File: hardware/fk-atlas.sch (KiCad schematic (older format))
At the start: 55 parts, among them J1 CONN-HDR-2x5, J2 MICRO-USB, J3 Conn_01x02, J4 Conn_01x09, M1 MOUNT_HOLE, M2 MOUNT_HOLE, M3 MOUNT_HOLE, M4 MOUNT_HOLE, Q1 2N7002LT1G, Q2 2N7002LT1G, Q3 2N7002LT1G, Q4 2N7002LT1G, Q5 2N7002LT1G, SW1 SPNO, U1 S25FL1xxK0XM, U2 ATSAMD21G18A-AU, U3 MCP1700T-3302E/MB, Y1 FC-135

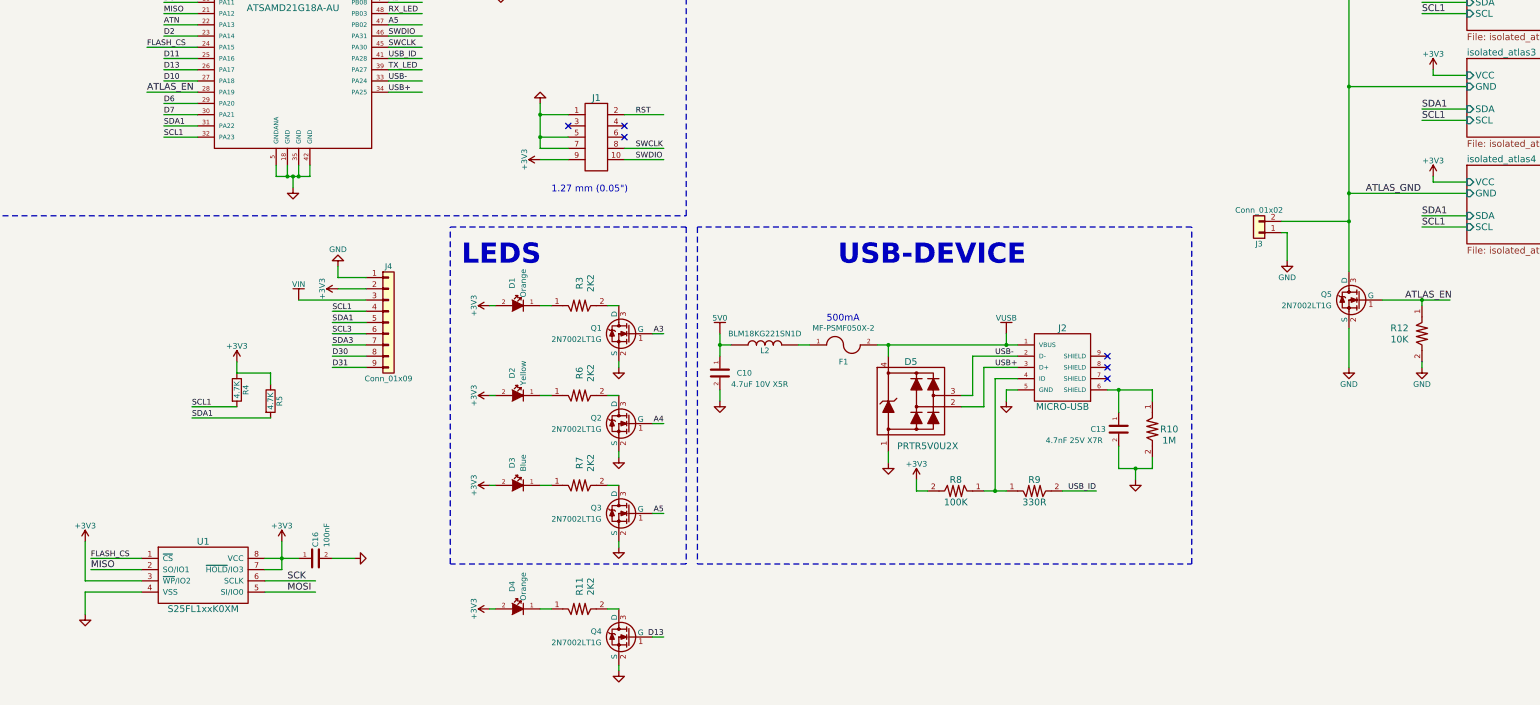
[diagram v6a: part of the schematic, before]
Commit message: Flash memory is on PERIPH_GND now too.
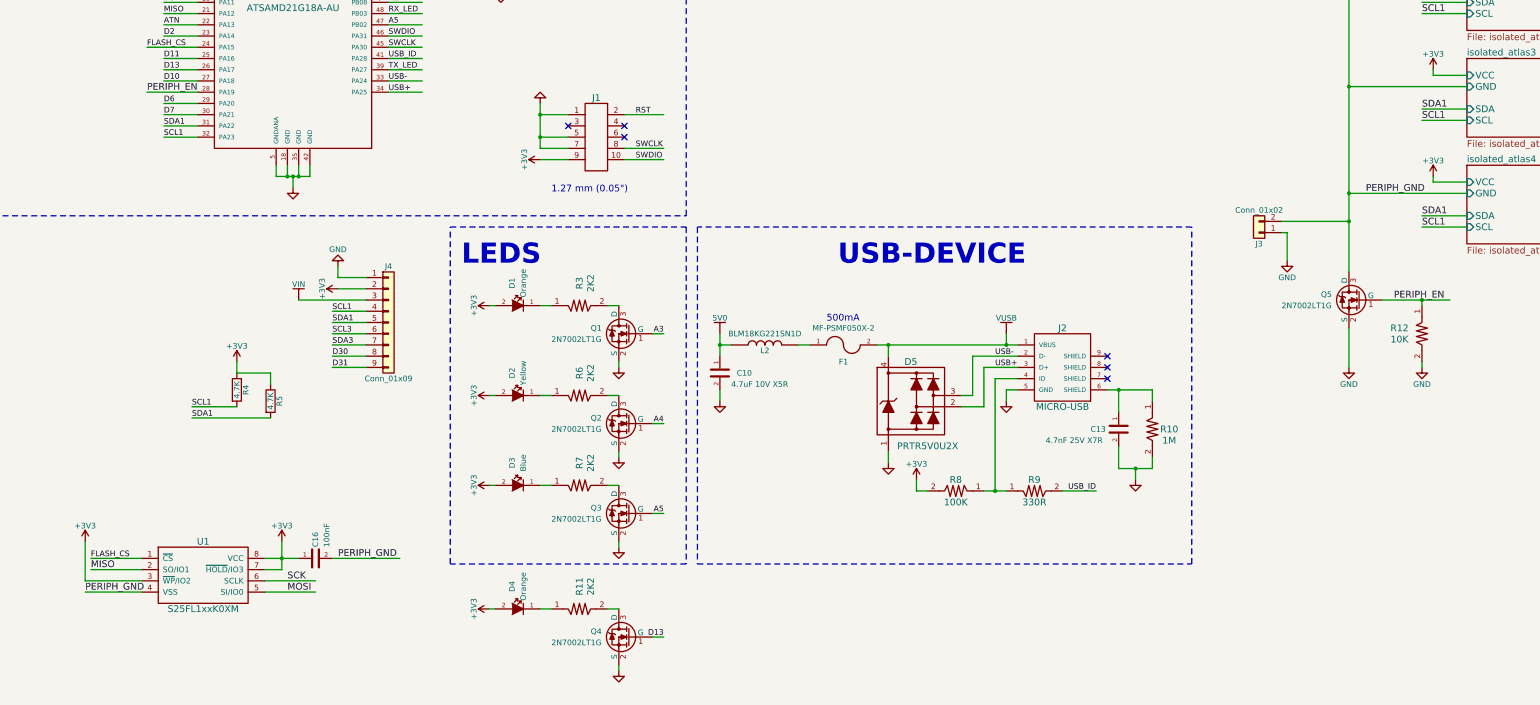
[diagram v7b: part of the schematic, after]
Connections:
- net labels added: PERIPH_EN, PERIPH_GND
- net labels removed: ATLAS_EN, ATLAS_GND
- wire segments 223 -> 222
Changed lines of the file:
@@
 LIBS:RocketScreamKicadLibrary
 LIBS:fk-atlas-cache
-LIBS:mounting-cache
 EELAYER 25 0
 EELAYER END
@@
 Wire Wire Line
 	13400 5850 14000 5850
-Text Label 13600 5850 0    60   ~ 0
-ATLAS_EN
+Text Label 13500 5850 0    60   ~ 0
+PERIPH_EN
 Text Label 2400 4000 0    60   ~ 0
-ATLAS_EN
+PERIPH_EN
 Wire Wire Line
 	13100 1100 14150 1100
@@
 	1    0    0    -1
 $EndComp
-$Comp
-L GND #PWR14
-U 1 1 5A1D1A01
-P 4250 8150
-F 0 "#PWR14" H 4250 7900 50  0001 C CNN
-F 1 "GND" H 4250 8000 50  0001 C CNN
-F 2 "" H 4250 8150 60  0000 C CNN
-F 3 "" H 4250 8150 60  0000 C CNN
-	1    4250 8150
-	0    -1   -1   0
-$EndComp
 Wire Wire Line
 	3600 8000 3600 8250
@@
 Connection ~ 3600 8150
 Wire Wire Line
-	4250 8150 4050 8150
+	4050 8150 4650 8150
 Wire Wire Line
 	3900 8350 3450 8350
@@
 	1    0    0    -1
 $EndComp
-$Comp
-L GND #PWR5
-U 1 1 5A1D26FC
-P 1850 8650
-F 0 "#PWR5" H 1850 8400 50  0001 C CNN
-F 1 "GND" H 1850 8500 50  0001 C CNN
-F 2 "" H 1850 8650 60  0000 C CNN
-F 3 "" H 1850 8650 60  0000 C CNN
-	1    1850 8650
-	1    0    0    -1
-$EndComp
 Wire Wire Line
 	1900 8250 2350 8250
@@
 Wire Wire Line
 	2350 8450 1850 8450
-Wire Wire Line
-	1850 8450 1850 8650
 Wire Wire Line
 	1850 8350 2350 8350
@@
 $EndComp
 Text Label 13250 4900 0    60   ~ 0
-ATLAS_GND
+PERIPH_GND
 Wire Wire Line
 	2550 3700 2850 3700
@@
 Wire Notes Line
 	2650 9750 550  9750
+Text Label 1850 8450 0    60   ~ 0
+PERIPH_GND
+Text Label 4100 8150 0    60   ~ 0
+PERIPH_GND
 $EndSCHEMATC

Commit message: Updating BOM details.
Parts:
- U1: spn1 (none) -> 797-25FL116KOXMFI041
